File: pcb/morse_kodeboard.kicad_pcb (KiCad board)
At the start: 2 copper layers, 53.5 x 55 mm, 7 parts, among them SW1 SW_DPST

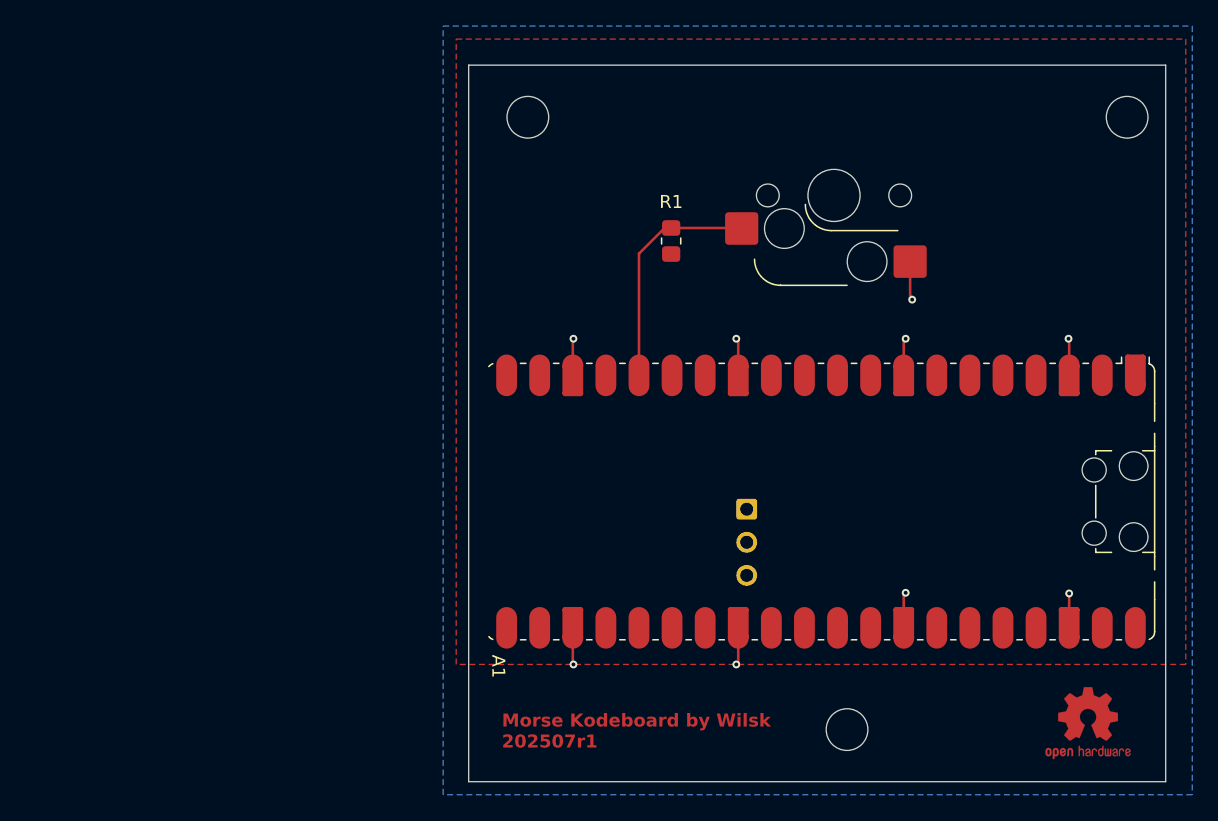
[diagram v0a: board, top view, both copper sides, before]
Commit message: Make PCB single button
Signed-off-by: William Hart <391950+will-hart@users.noreply.github.com>
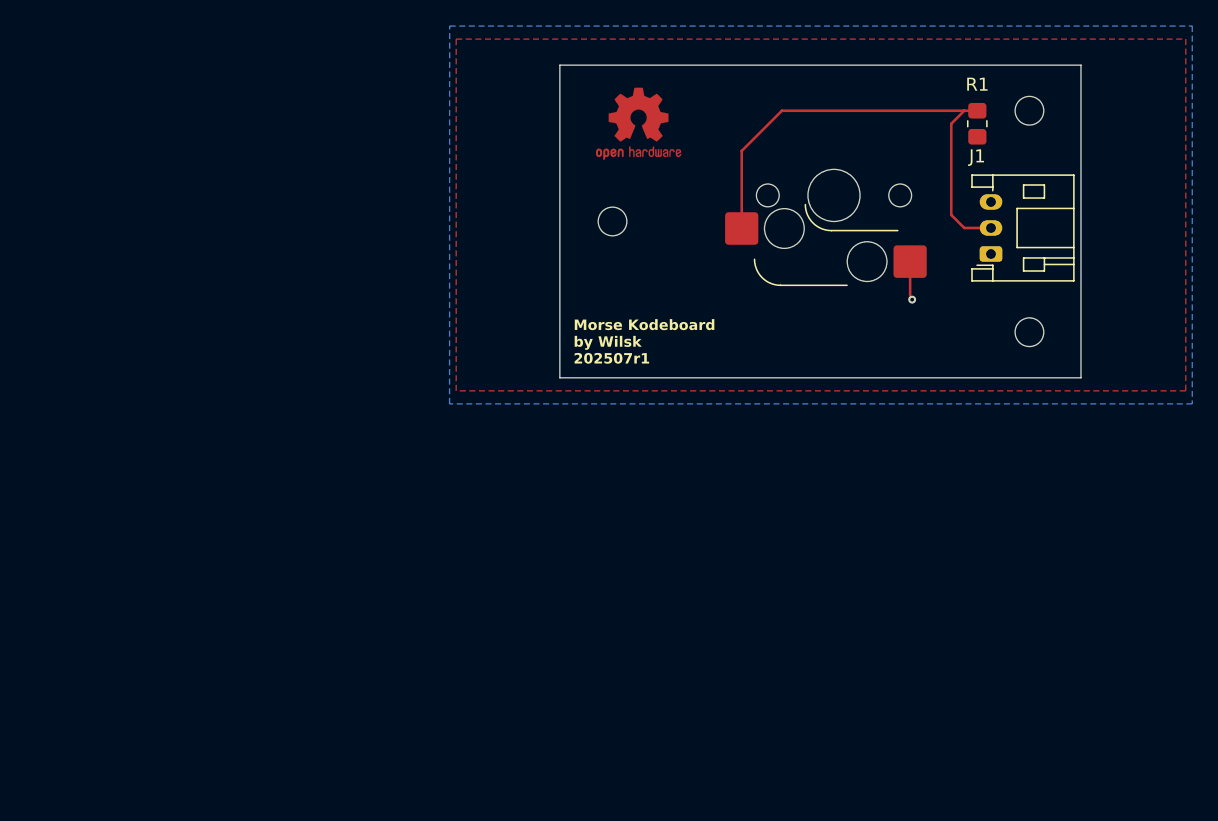
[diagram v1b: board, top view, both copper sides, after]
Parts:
- removed A1: RaspberryPi_Pico_W, Module:RaspberryPi_Pico_W_SMD_HandSolder
- added J1: Conn_01x03, Connector_JST:JST_PH_S3B-PH-K_1x03_P2.00mm_Horizontal, F.Cu at (185.1, 37.0)
- H1, H2, H3: footprint MountingHole:MountingHole_3.2mm_M3 -> MountingHole:MountingHole_2.2mm_M2
- moved SYM1 57.5 mm to (158.0, 27.0)
- moved H3 33.6 mm to (188.0, 43.0)
- moved R1 25.2 mm to (184.0, 27.0)
- moved H1 10.3 mm to (156.0, 34.5)
- moved H2 7.52 mm to (188.0, 26.0)
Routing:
- net GND: track 25.5 -> 2.99 mm, vias 9 -> 1
- net /SW1: track 18.1 -> 37.2 mm
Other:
- board size 53.5 x 55 mm -> 40 x 24 mm

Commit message: Update PCB files with three buttons.
Sent off to fab as r1!

Signed-off-by: William Hart <391950+will-hart@users.noreply.github.com>
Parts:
- added H4: MountingHole, MountingHole:MountingHole_2.2mm_M2, F.Cu at (189.0, 43.5)
- added R2: R_US, Resistor_SMD:R_0805_2012Metric_Pad1.20x1.40mm_HandSolder, F.Cu at (145.0, 44.0)
- added R3: R_US, Resistor_SMD:R_0805_2012Metric_Pad1.20x1.40mm_HandSolder, F.Cu at (123.0, 44.0)
- added SW2: SW_DPST, PCM_Switch_Keyboard_Hotswap_Kailh:SW_Hotswap_Kailh_MX_1.00u, B.Cu at (151.0, 32.5)
- added SW3: SW_DPST, PCM_Switch_Keyboard_Hotswap_Kailh:SW_Hotswap_Kailh_MX_1.00u, B.Cu at (129.0, 32.5)
- J1: footprint Connector_JST:JST_PH_S3B-PH-K_1x03_P2.00mm_Horizontal -> Connector_JST:JST_PH_S5B-PH-K_1x05_P2.00mm_Horizontal
- SYM1: moved to B.Cu
- moved H2 71.5 mm to (116.5, 25.0)
- moved H3 71.5 mm to (116.5, 43.5)
- moved SYM1 42.6 mm to (116.0, 34.0), turned to -90 degrees
- moved H1 34.3 mm to (189.0, 25.0)
- moved R1 24.5 mm to (165.9, 43.5), turned to 180 degrees
- moved J1 1.50 mm to (185.1, 38.5)
- moved SW1 1.00 mm to (172.0, 32.5)
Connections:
- J1 pad 3: GND -> /SW2
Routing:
- net /SW3: track 0.00 -> 85.0 mm
- net /SW2: track 0.00 -> 60.5 mm
- net GND: track 2.99 -> 8.73 mm, vias 1 -> 3
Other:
- board size 40 x 24 mm -> 79.5 x 26 mm
- board text added: "G"
- board text added: "MORSE"
- board text added: "SHIFT"
- board text added: "SPACE"
- board text added: "V"
